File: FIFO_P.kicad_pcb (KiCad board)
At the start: 4 copper layers, 100 x 100 mm, 74 parts, among them J1 Vin +, J2 Vin -, J3 ICLK, J4 Vout, J5 Jack-DC, SW1 Rotary_Encoder_61C, U1 SN74LVC2G157_MUX_TI, U10 AD7840, U11 LM2776, U12 LM2940CT-5.0, U13 LM2940CT-3.3, U2 IDT_ICS551, U3 LTC1740, U4 ARDUINO_DUE_FIFO_P_COMMANDS, U5 IDT_72V2105, U6 TXB0104, U7 TXB0104, U8 TXB0104, U9 TXB0104

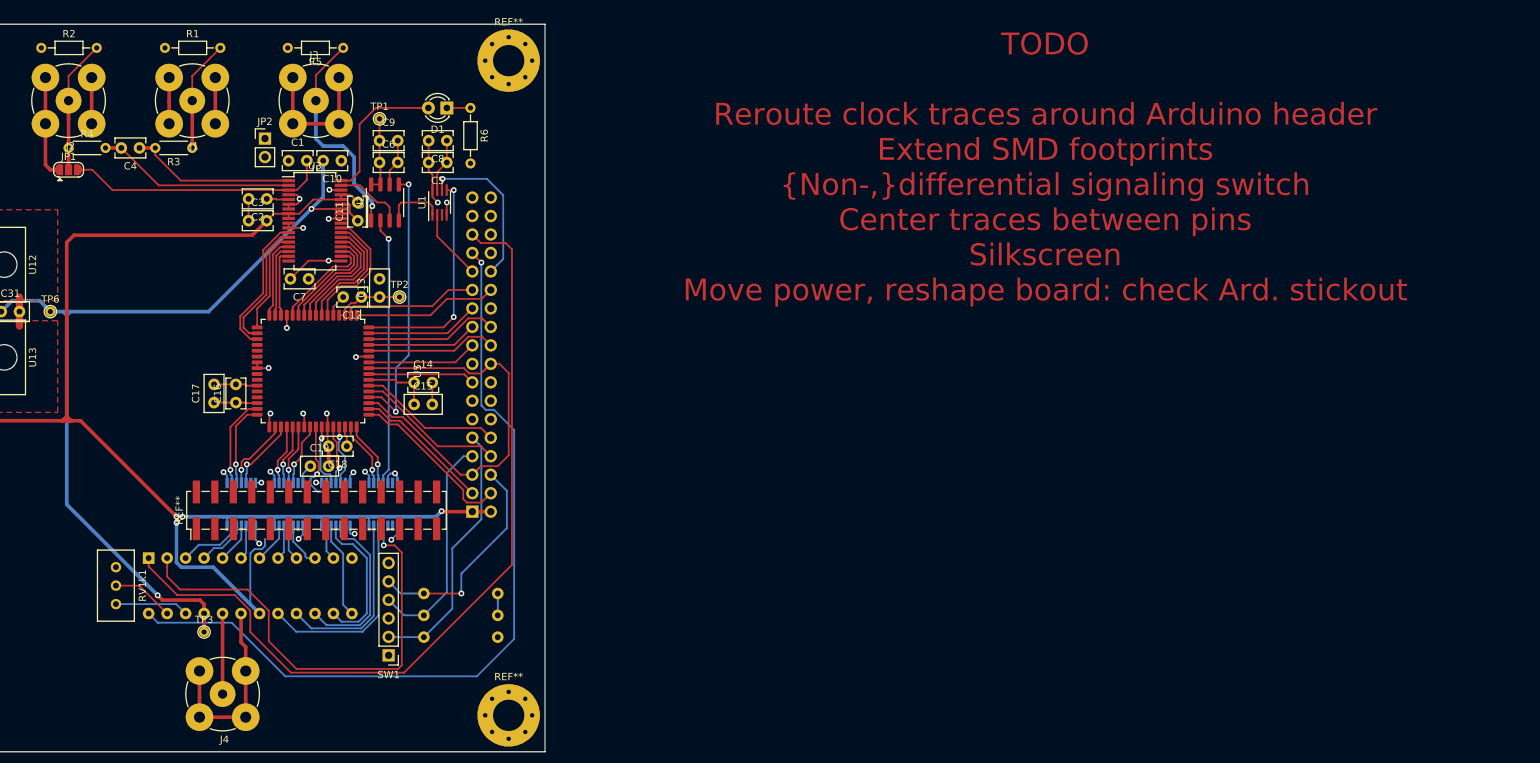
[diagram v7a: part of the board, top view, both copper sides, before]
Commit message: Routed FIFO-DAC header
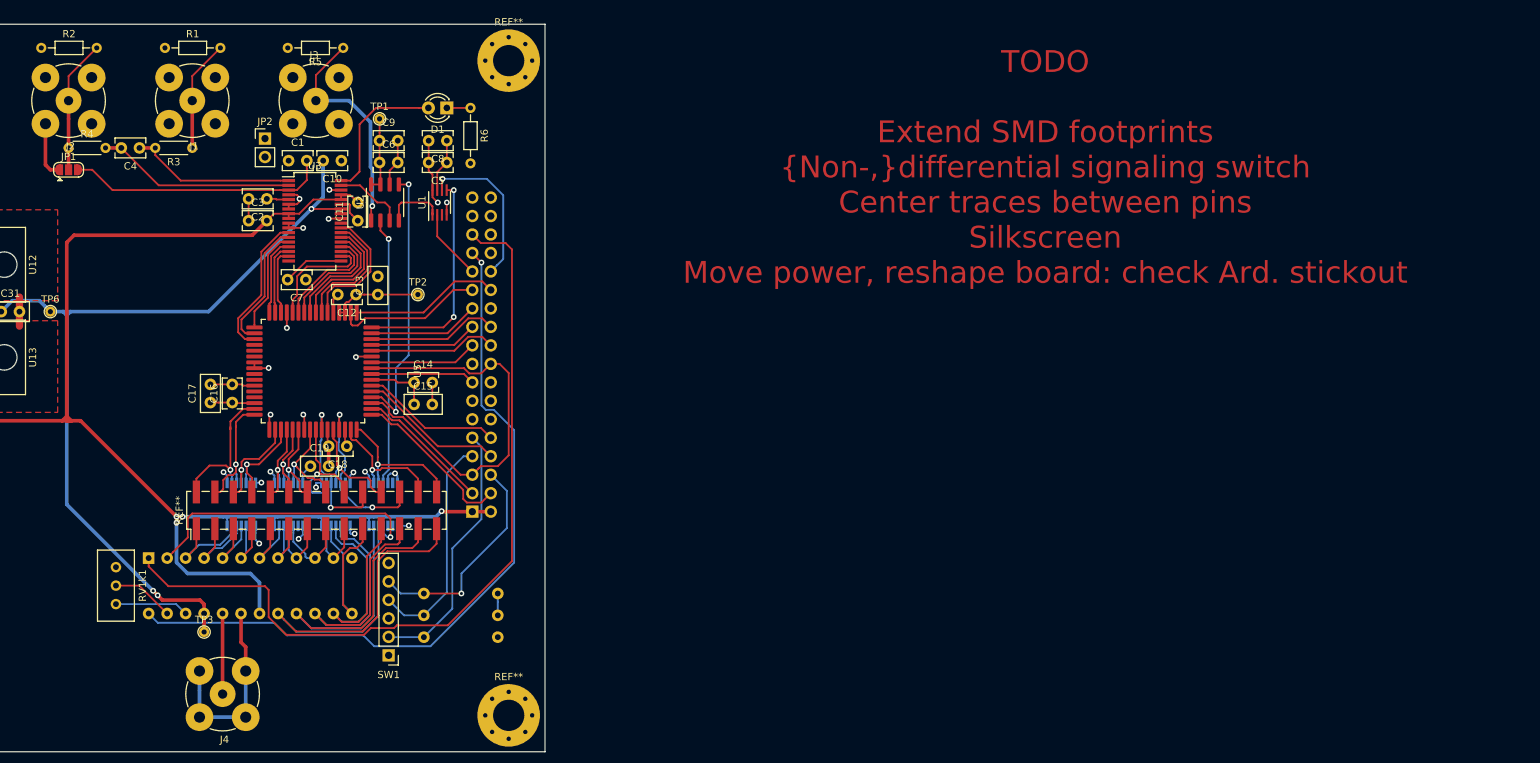
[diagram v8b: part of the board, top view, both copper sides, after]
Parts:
- U5: footprint Package_QFP:LQFP-64_14x14mm_P0.8mm -> FIFO_P:LQFP-64_14x14mm_P0.8mm_HandSolder
- moved TP2 2.54 mm to (132.0, 86.7)
- moved C12 0.81 mm to (123.5, 86.7)
- moved C16 0.50 mm to (106.5, 101.5)
- moved C17 0.50 mm to (103.5, 101.5)
- moved C13 0.42 mm to (126.5, 86.7)
- moved C7 0.40 mm to (116.6, 84.6)
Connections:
- REF** pad 1: (no net) -> Net-(U10-Pad3)
- REF** pad 10: (no net) -> Net-(U5-Pad36)
- REF** pad 11: (no net) -> Net-(U10-Pad8)
- REF** pad 12: (no net) -> Net-(U5-Pad37)
- REF** pad 13: (no net) -> Net-(U10-Pad9)
- REF** pad 14: (no net) -> Net-(U5-Pad38)
- REF** pad 15: (no net) -> Net-(U10-Pad10)
- REF** pad 16: (no net) -> Net-(U5-Pad40)
- REF** pad 17: (no net) -> Net-(U10-Pad11)
- REF** pad 18: (no net) -> Net-(U5-Pad41)
- REF** pad 19: (no net) -> Net-(U10-Pad13)
- REF** pad 2: (no net) -> Net-(U5-Pad31)
- REF** pad 20: (no net) -> Net-(U5-Pad42)
- REF** pad 21: (no net) -> Net-(U10-Pad14)
- REF** pad 22: (no net) -> Net-(U5-Pad44)
- REF** pad 23: (no net) -> Net-(U10-Pad15)
- REF** pad 24: (no net) -> Net-(U5-Pad45)
- REF** pad 25: (no net) -> Net-(U10-Pad16)
- REF** pad 26: (no net) -> Net-(U5-Pad47)
- REF** pad 27: (no net) -> Net-(U10-Pad17)
- REF** pad 28: (no net) -> Net-(U5-Pad48)
- REF** pad 3: (no net) -> Net-(U10-Pad4)
- REF** pad 4: (no net) -> Net-(U5-Pad32)
- REF** pad 5: (no net) -> Net-(U10-Pad5)
- REF** pad 6: (no net) -> Net-(U5-Pad34)
- REF** pad 7: (no net) -> Net-(U10-Pad6)
- REF** pad 8: (no net) -> Net-(U5-Pad35)
- REF** pad 9: (no net) -> Net-(U10-Pad7)
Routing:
- net Net-(U10-Pad17): track 28.1 -> 62.5 mm
- net Net-(U10-Pad16): track 24.6 -> 53.3 mm
- net GNDA: track 46.2 -> 20.8 mm
- net LDAC5V: track 63.8 -> 39.9 mm
- net Net-(U10-Pad15): track 23.6 -> 47.0 mm
- net GND: track 101.9 -> 83.8 mm
- net Net-(U10-Pad14): track 20.2 -> 38.2 mm
- net Net-(U5-Pad45): track 8.39 -> 24.5 mm, vias 1 -> 2
- net Net-(U10-Pad13): track 13.2 -> 27.9 mm
- net Net-(U5-Pad42): track 8.79 -> 22.3 mm, vias 1 -> 2
- net Net-(U5-Pad48): track 8.94 -> 19.6 mm
- net +5V: track 235.5 -> 225.8 mm
- net Net-(U10-Pad24): track 112.0 -> 102.5 mm
- net Net-(U5-Pad47): track 9.00 -> 17.8 mm
- net Net-(U5-Pad44): track 8.26 -> 16.6 mm
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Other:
- board text added: "TODO Extend SMD footprints {Non-,}differential signaling switch Center traces between pins Silkscreen Move power, reshape board: check Ard. stickout"
- board text removed: "TODO Reroute clock traces around Arduino header Extend SMD footprints {Non-,}differential signaling switch Center traces between pins Silkscreen Move power, reshape board: check Ard. stickout"
